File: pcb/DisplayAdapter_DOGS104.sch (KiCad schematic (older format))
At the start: 9 parts, among them J1 Conn_01x07_Male, U1 EA_DOGS104x-A

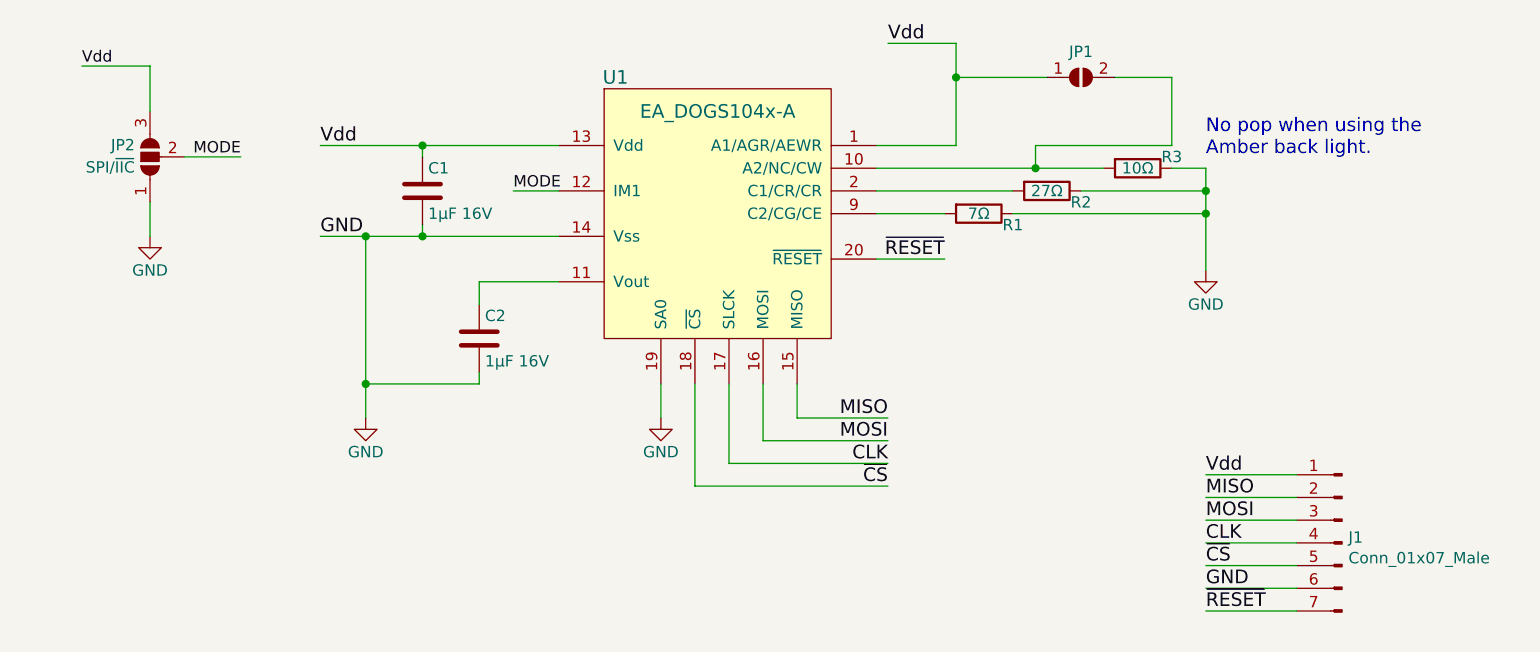
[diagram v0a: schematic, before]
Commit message: Adds IIC address capability Rev 4
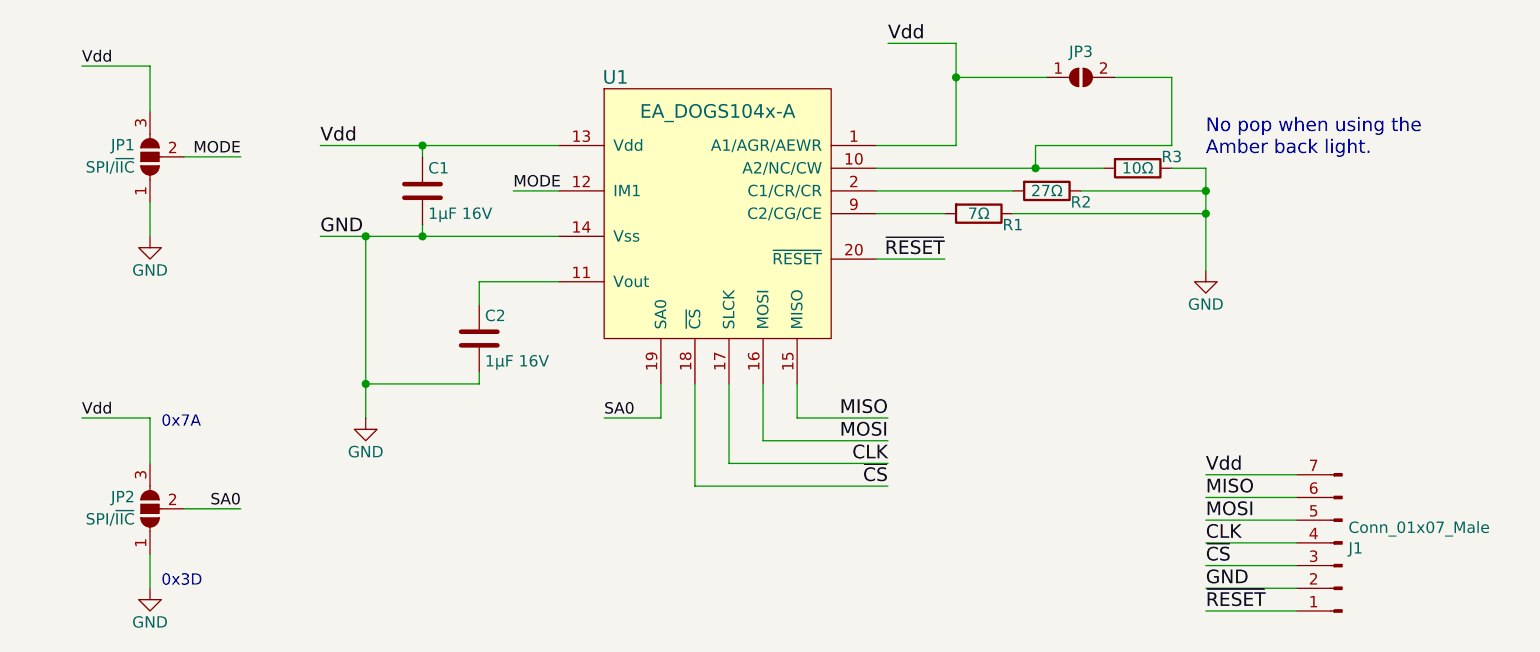
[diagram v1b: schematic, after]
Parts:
- added JP2: SPI/~IIC, Jumper:SolderJumper-3_P1.3mm_Open_RoundedPad1.0x1.5mm_NumberLabels, symbol Jumper:SolderJumper_3_Open
- C1, C2: footprint Capacitors_SMD:C_0805 -> Capacitor_SMD:C_0805_2012Metric_Pad1.15x1.40mm_HandSolder
- R1, R2, R3: footprint Resistors_SMD:R_0805_HandSoldering -> Resistor_SMD:R_0805_2012Metric_Pad1.15x1.40mm_HandSolder
- renumbered JP2 to JP1, JP1 to JP3
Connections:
- net GND: now also J1.2 (Pin_2), JP2.1 (A); no longer J1.6 (Pin_6), U1.19 (SA0~)
- net MISO: now also J1.6 (Pin_6); no longer J1.2 (Pin_2)
- net MOSI: now also J1.5 (Pin_5); no longer J1.3 (Pin_3)
- net Vdd: now also J1.7 (Pin_7), JP2.3 (B); no longer J1.1 (Pin_1)
- net ~CS: now also J1.3 (Pin_3); no longer J1.5 (Pin_5)
- net ~RESET: now also J1.1 (Pin_1); no longer J1.7 (Pin_7)
- new net SA0: JP2.2 (C), U1.19 (SA0~)
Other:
- note added: "0x3D"
- note added: "0x7A"
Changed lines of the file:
@@
 F 3 "~" H 8100 4550 50  0001 C CNN
 	1    8100 4550
-	-1   0    0    -1
-$EndComp
-$Comp
-L Jumper:SolderJumper_2_Open JP1
+	-1   0    0    1
+$EndComp
+$Comp
+L Jumper:SolderJumper_2_Open JP3
 U 1 1 5F2F74EA
 P 6950 2500
-F 0 "JP1" H 6950 2613 50  0000 C CNN
+F 0 "JP3" H 6950 2613 50  0000 C CNN
 F 1 "SolderJumper_2_Open" H 6950 2614 50  0001 C CNN
 F 2 "Jumper:SolderJumper-2_P1.3mm_Open_RoundedPad1.0x1.5mm" H 6950 2500 50  0001 C CNN
@@
 	6400 2350 6400 2500
 $Comp
-L power:GND #PWR03
+L power:GND #PWR04
 U 1 1 59F77332
 P 7500 3350
-F 0 "#PWR03" H 7500 3100 50  0001 C CNN
+F 0 "#PWR04" H 7500 3100 50  0001 C CNN
 F 1 "GND" H 7500 3200 50  0000 C CNN
 F 2 "" H 7500 3350 50  0001 C CNN
@@
 F 0 "R3" V 7150 3050 50  0000 C CNN
 F 1 "10Ω" V 7200 2900 50  0000 C CNN
-F 2 "Resistors_SMD:R_0805_HandSoldering" V 7130 2900 50  0001 C CNN
+F 2 "Resistor_SMD:R_0805_2012Metric_Pad1.15x1.40mm_HandSolder" V 7130 2900 50  0001 C CNN
 F 3 "" H 7200 2900 50  0001 C CNN
 	1    7200 2900
@@
 F 0 "R1" V 6550 3250 50  0000 C CNN
 F 1 "7Ω" V 6500 3100 50  0000 C CNN
-F 2 "Resistors_SMD:R_0805_HandSoldering" V 6430 3100 50  0001 C CNN
+F 2 "Resistor_SMD:R_0805_2012Metric_Pad1.15x1.40mm_HandSolder" V 6430 3100 50  0001 C CNN
 F 3 "" H 6500 3100 50  0001 C CNN
 	1    6500 3100
@@
 F 0 "R2" V 6850 3150 50  0000 C CNN
 F 1 "27Ω" V 6800 3000 50  0000 C CNN
-F 2 "Resistors_SMD:R_0805_HandSoldering" V 6730 3000 50  0001 C CNN
+F 2 "Resistor_SMD:R_0805_2012Metric_Pad1.15x1.40mm_HandSolder" V 6730 3000 50  0001 C CNN
 F 3 "" H 6800 3000 50  0001 C CNN
 F 4 "Value" H 6800 3000 60  0001 C CNN "Link"
@@
 Wire Wire Line
 	5100 3850 5100 4000
-$Comp
-L power:GND #PWR02
-U 1 1 59F72FDF
-P 5100 4000
-F 0 "#PWR02" H 5100 3750 50  0001 C CNN
-F 1 "GND" H 5100 3850 50  0000 C CNN
-F 2 "" H 5100 4000 50  0001 C CNN
-F 3 "" H 5100 4000 50  0001 C CNN
-	1    5100 4000
-	1    0    0    -1
-$EndComp
 Text Label 7500 4650 0    60   ~ 0
 ~CS
@@
 F 0 "C2" H 4325 3750 50  0000 L CNN
 F 1 "1μF 16V" H 4325 3550 50  0000 L CNN
-F 2 "Capacitors_SMD:C_0805" H 4338 3500 50  0001 C CNN
+F 2 "Capacitor_SMD:C_0805_2012Metric_Pad1.15x1.40mm_HandSolder" H 4338 3500 50  0001 C CNN
 F 3 "" H 4300 3650 50  0001 C CNN
 F 4 "Value" H 4300 3650 60  0001 C CNN "Link"
@@
 $EndComp
 $Comp
-L power:GND #PWR01
+L power:GND #PWR03
 U 1 1 59F72CC7
 P 3800 4000
-F 0 "#PWR01" H 3800 3750 50  0001 C CNN
+F 0 "#PWR03" H 3800 3750 50  0001 C CNN
 F 1 "GND" H 3800 3850 50  0000 C CNN
 F 2 "" H 3800 4000 50  0001 C CNN
@@
 F 0 "C1" H 4075 3100 50  0000 L CNN
 F 1 "1μF 16V" H 4075 2900 50  0000 L CNN
-F 2 "Capacitors_SMD:C_0805" H 4088 2850 50  0001 C CNN
+F 2 "Capacitor_SMD:C_0805_2012Metric_Pad1.15x1.40mm_HandSolder" H 4088 2850 50  0001 C CNN
 F 3 "" H 4050 3000 50  0001 C CNN
 F 4 "Value" H 4050 3000 60  0001 C CNN "Link"
@@
 	3600 2800 4050 2800
 $Comp
-L Jumper:SolderJumper_3_Open JP2
+L Jumper:SolderJumper_3_Open JP1
 U 1 1 5F8E3EEB
 P 2850 2850
-F 0 "JP2" V 2902 2917 50  0000 L CNN
+F 0 "JP1" V 2902 2917 50  0000 L CNN
 F 1 "SPI/~IIC" V 2804 2917 50  0000 L CNN
 F 2 "Jumper:SolderJumper-3_P1.3mm_Open_RoundedPad1.0x1.5mm_NumberLabels" H 2850 2850 50  0001 C CNN
@@
 MODE
 $Comp
-L power:GND #PWR04
+L power:GND #PWR01
 U 1 1 5F8EB1C8
 P 2850 3200
-F 0 "#PWR04" H 2850 2950 50  0001 C CNN
+F 0 "#PWR01" H 2850 2950 50  0001 C CNN
 F 1 "GND" H 2850 3050 50  0000 C CNN
 F 2 "" H 2850 3200 50  0001 C CNN
@@
 Text Label 2550 2450 0    50   ~ 0
 Vdd
+$Comp
+L Jumper:SolderJumper_3_Open JP2
+U 1 1 5F901FB3
+P 2850 4400
+F 0 "JP2" V 2902 4467 50  0000 L CNN
+F 1 "SPI/~IIC" V 2804 4467 50  0000 L CNN
+F 2 "Jumper:SolderJumper-3_P1.3mm_Open_RoundedPad1.0x1.5mm_NumberLabels" H 2850 4400 50  0001 C CNN
+F 3 "~" H 2850 4400 50  0001 C CNN
+	1    2850 4400
+	0    -1   -1   0
+$EndComp
+Wire Wire Line
+	3000 4400 3250 4400
+$Comp
+L power:GND #PWR02
+U 1 1 5F901FBF
+P 2850 4750
+F 0 "#PWR02" H 2850 4500 50  0001 C CNN
+F 1 "GND" H 2850 4600 50  0000 C CNN
+F 2 "" H 2850 4750 50  0001 C CNN
+F 3 "" H 2850 4750 50  0001 C CNN
+	1    2850 4750
+	1    0    0    -1
+$EndComp
+Wire Wire Line
+	2850 4600 2850 4750
+Wire Wire Line
+	2850 4200 2850 4000
+Wire Wire Line
+	2850 4000 2550 4000
+Text Label 2550 4000 0    50   ~ 0
+Vdd
+Wire Wire Line
+	5100 4000 4850 4000
+Text Label 4850 4000 0    50   ~ 0
+SA0
+Text Label 3250 4400 2    50   ~ 0
+SA0
+Text Notes 2900 4050 0    50   ~ 0
+0x7A
+Text Notes 2900 4750 0    50   ~ 0
+0x3D
 $EndSCHEMATC

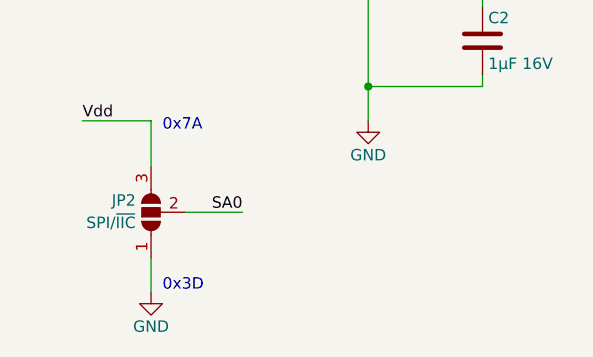
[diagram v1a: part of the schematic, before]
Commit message: Correction to the IIC address
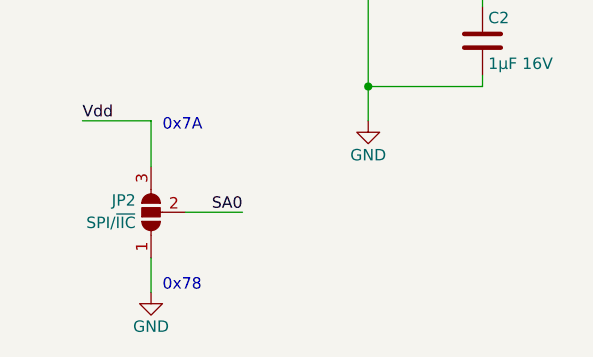
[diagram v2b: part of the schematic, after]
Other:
- note added: "0x78"
- note removed: "0x3D"
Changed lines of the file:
@@
 0x7A
 Text Notes 2900 4750 0    50   ~ 0
-0x3D
+0x78
 $EndSCHEMATC
